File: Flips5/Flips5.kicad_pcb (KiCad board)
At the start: 2 copper layers, 100 x 100 mm, 24 parts, among them IC1 FP2800A, IC2 FP2800A, IC3 FP2800A

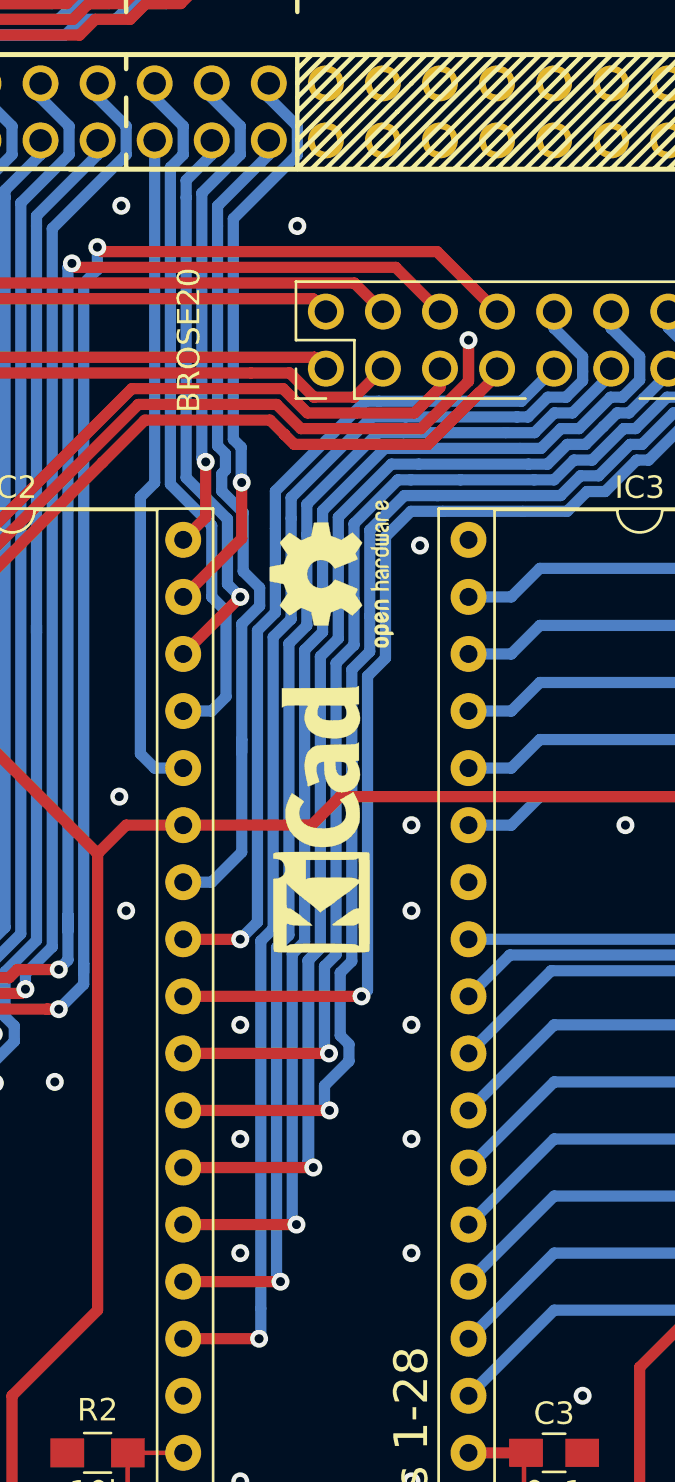
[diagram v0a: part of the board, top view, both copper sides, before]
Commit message: more ground plane friendly tracing
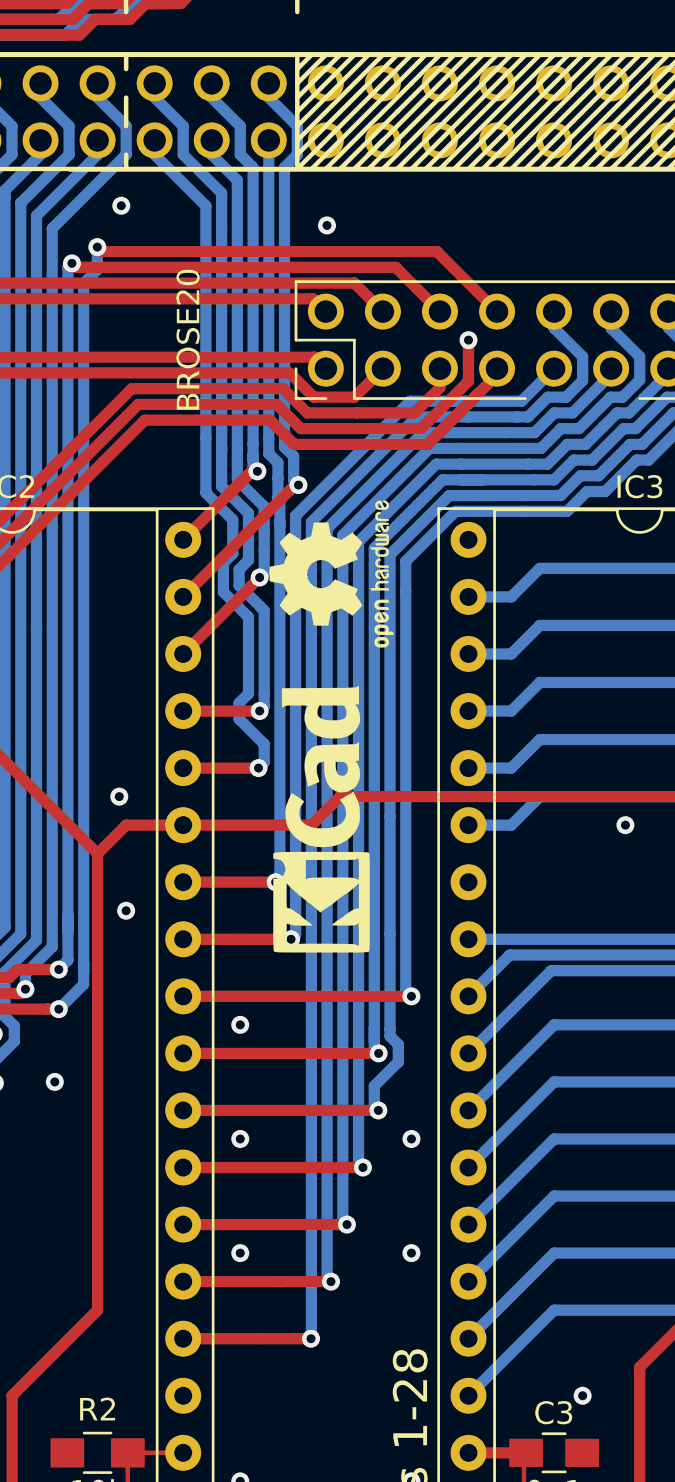
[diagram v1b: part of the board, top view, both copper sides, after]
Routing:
- net /~RY25: track 63.0 -> 53.0 mm
- net /~RY15: track 29.7 -> 34.1 mm, vias 0 -> 1
- net /~RY16: track 31.3 -> 34.1 mm, vias 0 -> 1
- net /~RY18: track 22.0 -> 24.5 mm
- net /~RY26: track 52.2 -> 53.9 mm
- net /~RY27: track 53.9 -> 52.6 mm
- net /~RY17: track 25.4 -> 26.0 mm
- net /~RY19: track 37.6 -> 37.4 mm, vias 0 -> 1
- net /GND: vias 93 -> 89

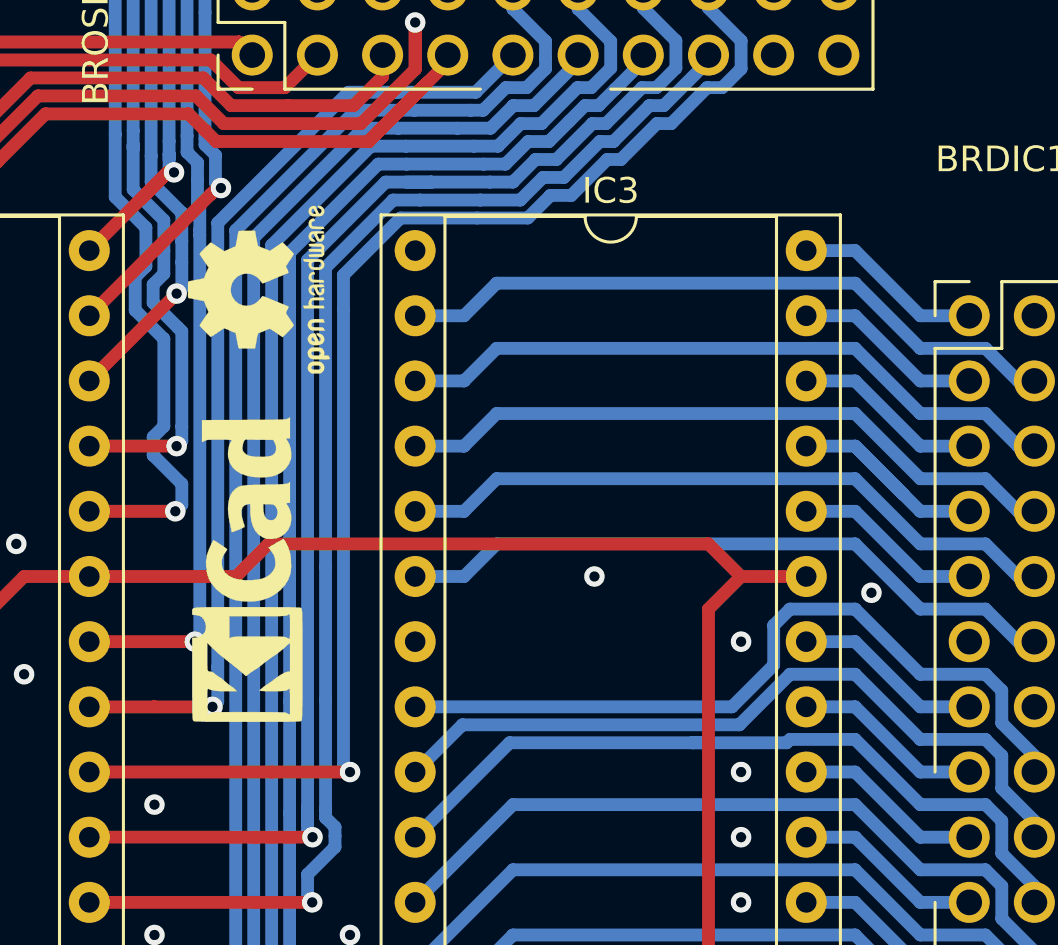
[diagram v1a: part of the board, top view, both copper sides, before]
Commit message: new placement of logos
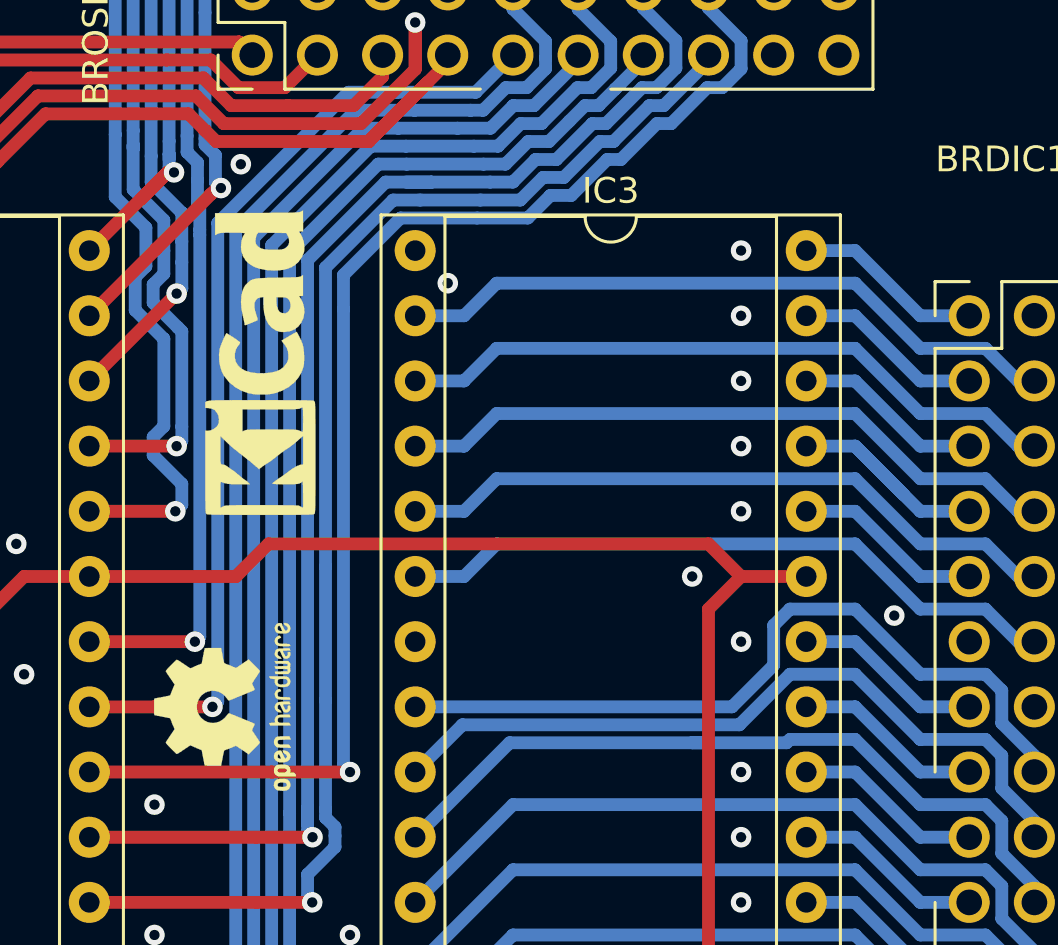
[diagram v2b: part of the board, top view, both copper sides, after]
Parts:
- moved REF*** 16.3 mm to (114.5, 104.1)
- moved REF** 8.08 mm to (115.7, 90.7)
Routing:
- net /GND: vias 89 -> 96
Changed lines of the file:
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@@
     (thickness 1.6)
     (drawings 110)
-    (tracks 1400)
+    (tracks 1407)
     (zones 0)
     (modules 24)
@@
   (layers
     (0 F.Cu signal)
-    (31 B.Cu signal)
+    (31 B.Cu signal hide)
     (32 B.Adhes user)
     (33 F.Adhes user)
     (34 B.Paste user)
     (35 F.Paste user)
-    (36 B.SilkS user hide)
-    (37 F.SilkS user hide)
+    (36 B.SilkS user)
+    (37 F.SilkS user)
     (38 B.Mask user)
-    (39 F.Mask user hide)
+    (39 F.Mask user)
     (40 Dwgs.User user)
     (41 Cmts.User user)
@@
   )
   (module Symbols:Symbol_KiCAD-Logo_CopperAndSilkScreenTop (layer F.Cu)
-    (at 115.189 98.806 90)
+    (at 115.697 90.7415 90)
     (descr "Symbol, KiCAD-Logo, Silk & Copper Top,")
     (tags "Symbol, KiCAD-Logo, Silk & Copper Top,")
@@
   )
   (module Symbols:OSHW-Logo2_7.3x6mm_SilkScreen (layer F.Cu)
-    (at 115.824 87.884 90)
+    (at 114.5032 104.14 90)
     (descr "Open Source Hardware Symbol")
     (tags "Logo Symbol OSHW")
@@
   (via (at 119.38 118.11) (size 0.8) (drill 0.4) (layers F.Cu B.Cu) (net 140))
   (via (at 119.38 113.03) (size 0.8) (drill 0.4) (layers F.Cu B.Cu) (net 140))
-  (via (at 128.905 99.06) (size 0.8) (drill 0.4) (layers F.Cu B.Cu) (net 140))
-  (via (at 139.7 99.695) (size 0.8) (drill 0.4) (layers F.Cu B.Cu) (net 140))
   (via (at 134.62 119.38) (size 0.8) (drill 0.4) (layers F.Cu B.Cu) (net 140))
   (via (at 134.62 116.84) (size 0.8) (drill 0.4) (layers F.Cu B.Cu) (net 140))
@@
   (via (at 95.377 89.916) (size 0.8) (drill 0.4) (layers F.Cu B.Cu) (net 140))
   (segment (start 95.631 90.17) (end 95.377 89.916) (width 0.5) (layer F.Cu) (net 140))
+  (via (at 134.62 96.52) (size 0.8) (drill 0.4) (layers F.Cu B.Cu) (net 140))
+  (via (at 134.62 93.98) (size 0.8) (drill 0.4) (layers F.Cu B.Cu) (net 140))
+  (via (at 134.62 91.44) (size 0.8) (drill 0.4) (layers F.Cu B.Cu) (net 140))
+  (via (at 134.62 88.9) (size 0.8) (drill 0.4) (layers F.Cu B.Cu) (net 140))
+  (via (at 134.62 86.36) (size 0.8) (drill 0.4) (layers F.Cu B.Cu) (net 140))
+  (via (at 123.19 87.63) (size 0.8) (drill 0.4) (layers F.Cu B.Cu) (net 140))
+  (via (at 132.715 99.06) (size 0.8) (drill 0.4) (layers F.Cu B.Cu) (net 140))
+  (via (at 140.589 100.584) (size 0.8) (drill 0.4) (layers F.Cu B.Cu) (net 140))
+  (via (at 115.1255 82.9945) (size 0.8) (drill 0.4) (layers F.Cu B.Cu) (net 140))
   (segment (start 129.54 123.19) (end 129.54 142.24) (width 0.5) (layer F.Cu) (net 141) (status 800020))
   (segment (start 133.35 119.38) (end 133.35 100.33) (width 0.5) (layer F.Cu) (net 141))
@@
     (polygon
       (pts
-        (xy 113.665 101.473) (xy 114.173 101.473) (xy 115.316 102.489) (xy 116.586 101.6) (xy 117.221 101.6)
-        (xy 117.221 104.521) (xy 116.586 104.648) (xy 114.046 104.648) (xy 113.665 104.521)
+        (xy 114.32286 93.57868) (xy 114.46002 93.71076) (xy 114.88166 94.10192) (xy 115.30838 94.42958) (xy 115.65128 94.70644)
+        (xy 115.8367 94.869) (xy 116.07546 94.69882) (xy 116.28882 94.55912) (xy 116.46916 94.41434) (xy 116.74094 94.2086)
+        (xy 116.9162 94.08414) (xy 117.0178 94.0181) (xy 117.20576 93.87586) (xy 117.29466 93.79966) (xy 117.38102 93.726)
+        (xy 117.46484 93.65234) (xy 117.5512 93.57106) (xy 117.55882 93.58376) (xy 117.55628 94.70898) (xy 117.475 94.70898)
+        (xy 117.40134 94.72422) (xy 117.29466 94.77248) (xy 117.16004 94.84868) (xy 116.96954 94.98076) (xy 116.78412 95.13062)
+        (xy 116.65712 95.21698) (xy 116.55806 95.27286) (xy 116.4971 95.32366) (xy 116.46154 95.34906) (xy 116.38788 95.41002)
+        (xy 116.36502 95.43796) (xy 116.41074 95.45066) (xy 116.62664 95.45828) (xy 116.99748 95.4659) (xy 117.2972 95.45574)
+        (xy 117.38356 95.4405) (xy 117.43436 95.42018) (xy 117.48516 95.38716) (xy 117.51564 95.3643) (xy 117.52834 95.3516)
+        (xy 117.53342 95.34906) (xy 117.54104 95.36938) (xy 117.54866 95.43288) (xy 117.5512 95.53448) (xy 117.54866 96.13646)
+        (xy 117.55628 96.3803) (xy 117.5512 96.38284) (xy 117.5004 96.36252) (xy 117.46992 96.34982) (xy 117.41658 96.32442)
+        (xy 117.38102 96.3041) (xy 117.28196 96.29902) (xy 117.03304 96.2914) (xy 115.97132 96.28124) (xy 114.99596 96.28886)
+        (xy 114.76228 96.28886) (xy 114.60734 96.29394) (xy 114.5159 96.30664) (xy 114.47526 96.32188) (xy 114.4016 96.35236)
+        (xy 114.3635 96.37268) (xy 114.33048 96.38538) (xy 114.32794 96.36506) (xy 114.32032 96.2279) (xy 114.32032 95.74022)
+        (xy 114.32032 95.54464) (xy 114.33048 95.41764) (xy 114.34064 95.38716) (xy 114.35334 95.36938) (xy 114.38382 95.377)
+        (xy 114.46256 95.41002) (xy 114.63528 95.44812) (xy 114.7826 95.45828) (xy 115.02898 95.46336) (xy 115.46332 95.46082)
+        (xy 115.4684 95.46082) (xy 115.40744 95.39986) (xy 115.35664 95.3516) (xy 115.316 95.32112) (xy 115.2525 95.28302)
+        (xy 115.08994 95.15602) (xy 114.94008 95.0214) (xy 114.89436 94.98076) (xy 114.65306 94.8182) (xy 114.53876 94.73692)
+        (xy 114.47272 94.71152) (xy 114.39652 94.70644) (xy 114.36096 94.68612) (xy 114.34572 94.65564) (xy 114.3254 94.55404)
+        (xy 114.32286 94.34576) (xy 114.32286 93.9165)
       )
     )

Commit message: adding pinout
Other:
- board text added: "11 13 10 9 8 12 14 7 5 6 4 3 2 1"
- board text added: "18 20 17 16 15 19 21 28 26 27 25 24 23 22"
- board text added: "A0"
- board text added: "A1"
- board text added: "A2"
- board text added: "B0"
- board text added: "B1"
- board text added: "DA"
- board text added: "EN"
- board text added: "GND"
- board text added: "SY1"
- board text added: "SY2"
- board text added: "SY21"
- board text added: "SY27"
- board text added: "SY28"
- board text added: "SY7"
- board text added: "VCC"
- board text added: "VS"
- board text added: "~RY1"
- board text added: "~RY19"
- board text added: "~RY1~ SY19"
- board text added: "~RY20"
- board text added: "~RY21"
- board text added: "~RY22"
- board text added: "~RY27"
- board text added: "~RY28"
- board text added: "~RY2~ SY20"
- board text added: "~RY7"
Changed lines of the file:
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@@
   (general
     (thickness 1.6)
-    (drawings 110)
+    (drawings 168)
     (tracks 1407)
     (zones 0)
@@
   )
   (layers
-    (0 F.Cu signal)
+    (0 F.Cu signal hide)
     (31 B.Cu signal hide)
     (32 B.Adhes user)
@@
     (35 F.Paste user)
     (36 B.SilkS user)
-    (37 F.SilkS user)
+    (37 F.SilkS user hide)
     (38 B.Mask user)
     (39 F.Mask user)
@@
     (solder_mask_min_width 0.25)
     (aux_axis_origin 0 0)
-    (grid_origin 50.8 50.8)
     (visible_elements 7FFFFFFF)
     (pcbplotparams
@@
     )
   )
+  (gr_line (start 120.904 146.812) (end 123.19 145.542) (layer B.SilkS) (width 0.2))
+  (gr_line (start 124.968 146.812) (end 125.984 145.796) (layer B.SilkS) (width 0.2))
+  (gr_line (start 134.112 146.812) (end 133.096 145.796) (layer B.SilkS) (width 0.2))
+  (gr_line (start 138.176 146.812) (end 135.89 145.542) (layer B.SilkS) (width 0.2))
+  (gr_line (start 129.54 146.812) (end 129.54 146.05) (layer B.SilkS) (width 0.2))
+  (gr_text A2 (at 120.65 148.082) (layer B.SilkS)
+    (effects (font (size 1.5 1.5) (thickness 0.3)) (justify mirror))
+  )
+  (gr_text B0 (at 138.43 148.082) (layer B.SilkS)
+    (effects (font (size 1.5 1.5) (thickness 0.3)) (justify mirror))
+  )
+  (gr_text DA (at 134.62 148.082) (layer B.SilkS)
+    (effects (font (size 1.5 1.5) (thickness 0.3)) (justify mirror))
+  )
+  (gr_text A1 (at 125.095 148.082) (layer B.SilkS)
+    (effects (font (size 1.5 1.5) (thickness 0.3)) (justify mirror))
+  )
+  (gr_text GND (at 129.54 148.082) (layer B.SilkS)
+    (effects (font (size 1.5 1.5) (thickness 0.3)) (justify mirror))
+  )
+  (gr_text A0 (at 120.65 138.938) (layer B.SilkS)
+    (effects (font (size 1.5 1.5) (thickness 0.3)) (justify mirror))
+  )
+  (gr_text VS (at 129.54 138.938) (layer B.SilkS)
+    (effects (font (size 1.5 1.5) (thickness 0.3)) (justify mirror))
+  )
+  (gr_text EN (at 134.62 138.938) (layer B.SilkS)
+    (effects (font (size 1.5 1.5) (thickness 0.3)) (justify mirror))
+  )
+  (gr_text B1 (at 138.43 138.938) (layer B.SilkS)
+    (effects (font (size 1.5 1.5) (thickness 0.3)) (justify mirror))
+  )
+  (gr_line (start 129.54 140.97) (end 129.54 140.208) (layer B.SilkS) (width 0.2))
+  (gr_line (start 125.984 141.224) (end 124.968 140.208) (layer B.SilkS) (width 0.2))
+  (gr_line (start 135.89 141.478) (end 138.176 140.208) (layer B.SilkS) (width 0.2))
+  (gr_line (start 133.096 141.224) (end 134.112 140.208) (layer B.SilkS) (width 0.2))
+  (gr_line (start 123.19 141.478) (end 120.904 140.208) (layer B.SilkS) (width 0.2))
+  (gr_text VCC (at 125.095 138.938) (layer B.SilkS)
+    (effects (font (size 1.5 1.5) (thickness 0.3)) (justify mirror))
+  )
+  (gr_text "11\n13\n10\n9\n8\n\n12\n14\n7\n5\n6\n4\n3\n2\n1" (at 147.32 109.22) (layer B.SilkS)
+    (effects (font (size 1.5 1.5) (thickness 0.3)) (justify right mirror))
+  )
+  (gr_text "18\n20\n17\n16\n15\n\n19\n21\n28\n26\n27\n25\n24\n23\n22" (at 142.24 106.68) (layer B.SilkS)
+    (effects (font (size 1.5 1.5) (thickness 0.3)) (justify left mirror))
+  )
+  (gr_line (start 133.35 74.93) (end 133.35 74.295) (layer B.SilkS) (width 0.2))
+  (gr_text ~RY28 (at 132.08 73.025) (layer B.SilkS)
+    (effects (font (size 1.5 1.5) (thickness 0.3)) (justify right mirror))
+  )
+  (gr_line (start 125.73 74.93) (end 125.73 74.295) (layer B.SilkS) (width 0.2))
+  (gr_line (start 123.19 74.93) (end 123.19 74.295) (layer B.SilkS) (width 0.2))
+  (gr_text SY28 (at 123.825 73.025) (layer B.SilkS)
+    (effects (font (size 1.5 1.5) (thickness 0.3)) (justify left mirror))
+  )
+  (gr_text ~RY22 (at 124.46 73.025) (layer B.SilkS)
+    (effects (font (size 1.5 1.5) (thickness 0.3)) (justify right mirror))
+  )
+  (gr_line (start 133.35 80.01) (end 133.35 80.645) (layer B.SilkS) (width 0.2))
+  (gr_line (start 125.73 80.01) (end 125.73 80.645) (layer B.SilkS) (width 0.2))
+  (gr_text ~RY27 (at 135.255 82.55) (layer B.SilkS)
+    (effects (font (size 1.5 1.5) (thickness 0.3)) (justify mirror))
+  )
+  (gr_text ~RY21 (at 124.46 82.55) (layer B.SilkS)
+    (effects (font (size 1.5 1.5) (thickness 0.3)) (justify right mirror))
+  )
+  (gr_line (start 123.19 80.01) (end 123.19 81.28) (layer B.SilkS) (width 0.2))
+  (gr_text SY27 (at 124.46 82.55) (layer B.SilkS)
+    (effects (font (size 1.5 1.5) (thickness 0.3)) (justify left mirror))
+  )
+  (gr_line (start 115.57 80.01) (end 115.57 81.28) (layer B.SilkS) (width 0.2))
+  (gr_text SY21 (at 116.84 82.55) (layer B.SilkS)
+    (effects (font (size 1.5 1.5) (thickness 0.3)) (justify left mirror))
+  )
+  (gr_text SY7 (at 119.38 61.595) (layer B.SilkS)
+    (effects (font (size 1.5 1.5) (thickness 0.3)) (justify mirror))
+  )
+  (gr_text SY1 (at 104.14 61.595) (layer B.SilkS)
+    (effects (font (size 1.5 1.5) (thickness 0.3)) (justify mirror))
+  )
+  (gr_line (start 104.14 59.69) (end 104.14 60.325) (layer B.SilkS) (width 0.2))
+  (gr_line (start 119.38 59.69) (end 119.38 60.325) (layer B.SilkS) (width 0.2))
+  (gr_line (start 119.38 54.61) (end 119.38 53.975) (layer B.SilkS) (width 0.2))
+  (gr_text ~RY7 (at 119.38 52.705) (layer B.SilkS)
+    (effects (font (size 1.5 1.5) (thickness 0.3)) (justify mirror))
+  )
+  (gr_line (start 104.14 53.975) (end 104.14 54.61) (layer B.SilkS) (width 0.2))
+  (gr_text ~RY1 (at 104.14 52.705) (layer B.SilkS)
+    (effects (font (size 1.5 1.5) (thickness 0.3)) (justify mirror))
+  )
+  (gr_line (start 113.03 64.77) (end 113.03 64.135) (layer B.SilkS) (width 0.2))
+  (gr_text ~RY20 (at 113.03 62.865) (layer B.SilkS)
+    (effects (font (size 1.5 1.5) (thickness 0.3)) (justify mirror))
+  )
+  (gr_line (start 113.03 69.85) (end 113.03 70.485) (layer B.SilkS) (width 0.2))
+  (gr_text ~RY19 (at 113.03 72.39) (layer B.SilkS)
+    (effects (font (size 1.5 1.5) (thickness 0.3)) (justify mirror))
+  )
+  (gr_line (start 64.77 64.77) (end 64.77 64.135) (layer B.SilkS) (width 0.2))
+  (gr_line (start 87.63 64.77) (end 87.63 64.135) (layer B.SilkS) (width 0.2))
+  (gr_line (start 90.17 64.77) (end 90.17 64.135) (layer B.SilkS) (width 0.2))
+  (gr_text "~RY2~ SY20" (at 88.265 62.865) (layer B.SilkS)
+    (effects (font (size 1.5 1.5) (thickness 0.3)) (justify mirror))
+  )
+  (gr_line (start 64.77 69.85) (end 64.77 71.12) (layer B.SilkS) (width 0.2))
+  (gr_line (start 90.17 69.85) (end 90.17 70.485) (layer B.SilkS) (width 0.2))
+  (gr_line (start 87.63 69.85) (end 87.63 71.12) (layer B.SilkS) (width 0.2))
+  (gr_text "~RY1~ SY19" (at 88.265 72.39) (layer B.SilkS)
+    (effects (font (size 1.5 1.5) (thickness 0.3)) (justify mirror))
+  )
+  (gr_text SY2 (at 64.77 62.865) (layer B.SilkS)
+    (effects (font (size 1.5 1.5) (thickness 0.3)) (justify mirror))
+  )
+  (gr_text SY1 (at 64.77 72.39) (layer B.SilkS)
+    (effects (font (size 1.5 1.5) (thickness 0.3)) (justify mirror))
+  )
   (dimension 5 (width 0.3) (layer Dwgs.User)

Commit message: Prepare release
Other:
- board text added: "SRT Flips 5 V1.0 2018-11-23 github.com/cawapy/FlipSuite"
- board text removed: "1"
- board text removed: "2"
- board text removed: "40"
- board text removed: "SRT Flips 5 V0.9 2018-11-16 github.com/cawapy/FlipSuite"
- board text removed: "Y-1 Y-2"

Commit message: fixing huge solder mask spacing
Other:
- rule pad_to_mask_clearance: 0.2 -> 0.051
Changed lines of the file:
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@@
     (pad_size 1.6 1.6)
     (pad_drill 0.8)
-    (pad_to_mask_clearance 0.2)
+    (pad_to_mask_clearance 0.051)
     (solder_mask_min_width 0.25)
     (aux_axis_origin 0 0)
